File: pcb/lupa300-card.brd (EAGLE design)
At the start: 45.7 x 76.5 mm, 22 parts

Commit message: more work on lupa card
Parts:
- added C13, C14, C15, C16, C17, C18, C19, C20, C21, C22, C25, C26, C27, C28, C29, C30, C5, C6: (no value), rcl:C0603
- added C23, C24: (no value), rcl:C1206
- moved C7 18.8 mm to (19.1, 51.4), turned to 90 degrees
- moved R7 17.9 mm to (20.3, 51.4), turned to 90 degrees
- moved U$2 8.35 mm to (40.0, 71.8)
- moved U$4 8.28 mm to (36.2, 64.1)
- moved C2 7.24 mm to (32.4, 72.4)
- moved C1 7.24 mm to (32.4, 69.8)
- moved U$1 2.54 mm to (15.2, 30.5)
- moved U$3 1.27 mm to (37.5, 55.9)
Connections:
- new net N$2: C25.2, C27.2
- net 2.5V: now also U$1.P$10, U$1.P$2, U$1.P$4, U$1.P$8
- net GND: now also C13.2, C14.2, C15.2, C16.2, C17.2, C18.2, C19.2, C20.2, C21.2, C22.2, C23.2, C24.2, C26.2, C28.2, C29.2, C30.2, C5.2, C6.2
- net VADC: now also C20.1, C21.1, C22.1; no longer U$1.P$4
- net VDDA: now also C14.1, C15.1, C16.1; no longer U$1.P$8
- net VDDD: now also C13.1, C5.1, C6.1; no longer U$1.P$10
- net VDDO: now also C17.1, C18.1, C19.1; no longer U$1.P$2
- net VPIX: now also C25.1, C26.1, C27.1
- net VRAW: now also C23.1, C24.1
- net VRESET_1: now also C28.1, C29.1, C30.1

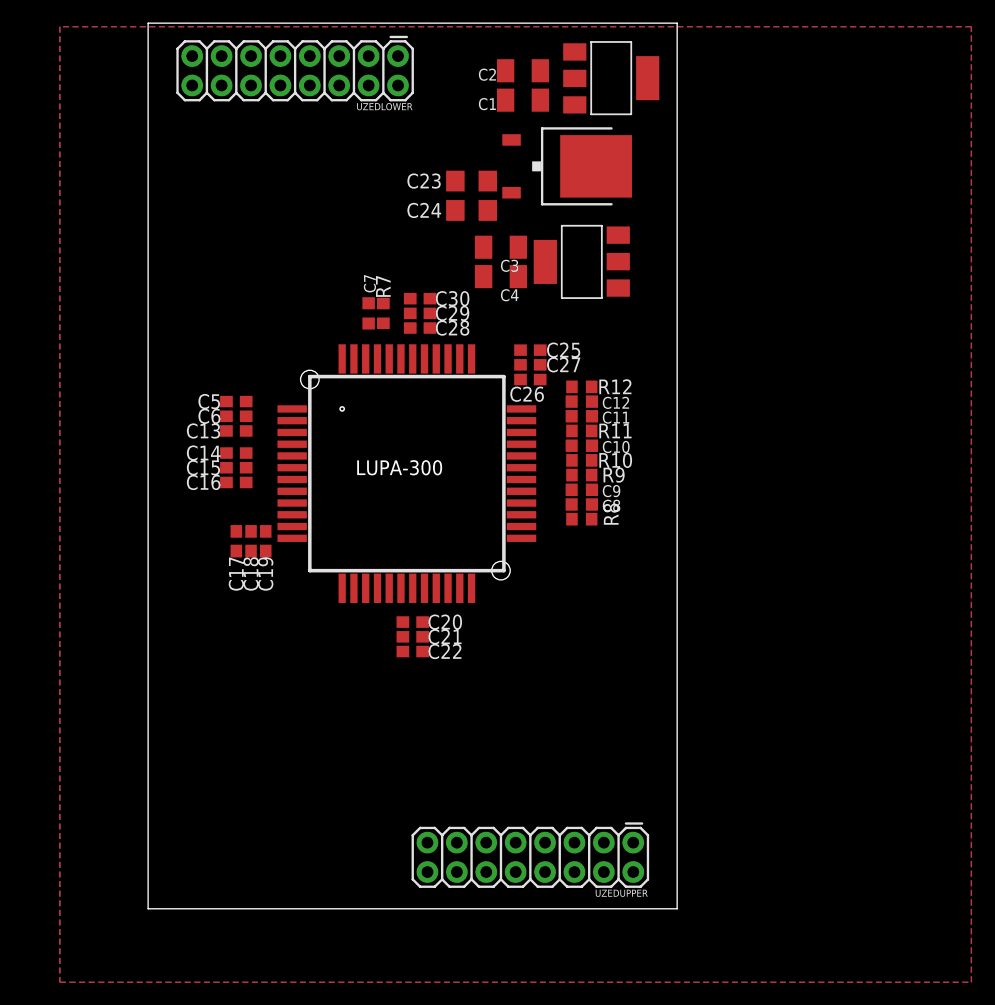
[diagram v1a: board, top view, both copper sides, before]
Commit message: made lupa card 4 layer
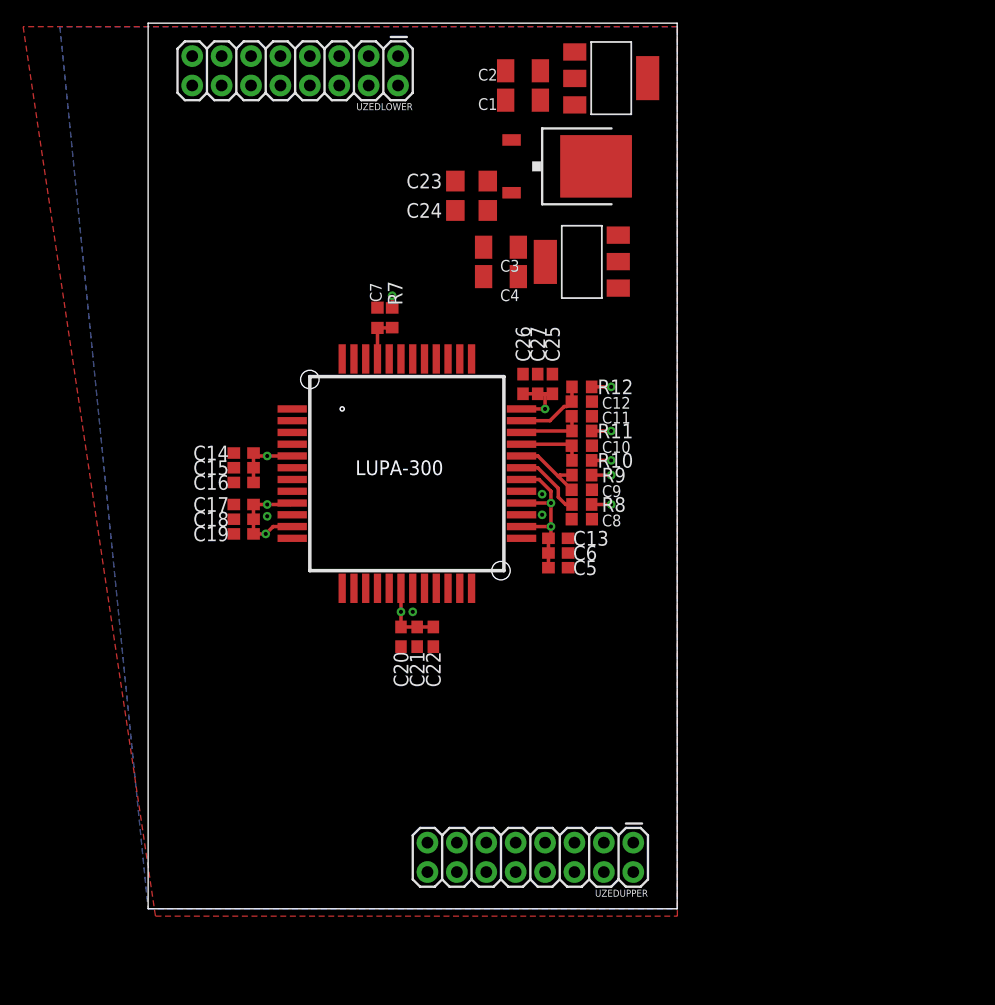
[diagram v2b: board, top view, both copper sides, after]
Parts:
- removed C28, C29, C30: (no value), rcl:C0603
- moved C5 31.3 mm to (35.4, 29.5), turned to 0 degrees
- moved C6 30.2 mm to (35.4, 30.7), turned to 0 degrees
- moved C13 29.3 mm to (35.4, 32.0), turned to 0 degrees
- moved C25 3.49 mm to (34.9, 45.3), turned to 90 degrees
- moved C17 3.24 mm to (8.26, 34.9), turned to 180 degrees
- moved C22 2.18 mm to (24.6, 23.5), turned to 270 degrees
- moved C18 2.01 mm to (8.26, 33.7), turned to 180 degrees
- moved C19 2.01 mm to (8.26, 32.4), turned to 180 degrees
- moved C27 1.77 mm to (33.7, 45.3), turned to 90 degrees
- moved C20 1.63 mm to (21.8, 23.5), turned to 270 degrees
- moved C8 1.27 mm to (37.5, 33.7)
- moved R8 1.27 mm to (37.5, 34.9)
- moved C7 0.85 mm to (19.8, 51.1)
- moved R7 0.85 mm to (21.1, 51.1), turned to 270 degrees
- moved C26 0.74 mm to (32.4, 45.3), turned to 90 degrees
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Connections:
- removed net N$2: C25.2, C27.2
- removed net VADC: C20.1, C21.1, C22.1, R8.1, U$1.P$21, U$1.P$30
- removed net VDDA: C14.1, C15.1, C16.1, R10.1, R11.1, R12.1, R9.1, U$1.P$19
- removed net VDDD: C13.1, C5.1, C6.1, U$1.P$23
- removed net VDDO: C17.1, C18.1, C19.1
- removed net VMEM_H: U$1.P$45
- removed net VPIX: C25.1, C26.1, C27.1, R7.1, U$1.P$13
- removed net VRESET_1: C28.1, C29.1, C30.1, U$1.P$43
- net 2.5V: now also C13.1, C14.1, C15.1, C16.1, C17.1, C18.1, C19.1, C20.1, C21.1, C22.1, C25.1, C26.1, C27.1, C5.1, C6.1, R10.1, R11.1, R12.1, R7.1, R8.1, R9.1, U$1.P$13, U$1.P$19, U$1.P$21, U$1.P$23, U$1.P$30
- net 3V3: now also U$1.P$43, U$1.P$45
- net GND: now also C25.2, C27.2; no longer C28.2, C29.2, C30.2
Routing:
- net 2.5V: track 0.00 -> 51.8 mm, vias 0 -> 13
- net BIAS4: track 0.00 -> 6.77 mm
- net BIAS1: track 0.00 -> 6.30 mm
- net ADC_BIAS: track 0.00 -> 6.12 mm
- net BIAS2: track 0.00 -> 5.69 mm
- net BIAS3: track 0.00 -> 5.66 mm
- net PRECHARGE_BIAS: track 0.00 -> 3.96 mm
- added copper zone on layer 2, net 2.5V
- added copper zone on layer 15, net 3V3

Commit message: finished prelim routing.
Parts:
- moved UZEDLOWER 67.9 mm to (21.5, 5.71)
- moved U$2 56.2 mm to (19.7, 19.3)
- moved U$4 55.2 mm to (17.7, 12.2)
- moved C23 55.1 mm to (8.13, 11.4), turned to 90 degrees
- moved C24 52.0 mm to (10.3, 11.4), turned to 90 degrees
- moved C2 50.2 mm to (19.2, 24.0)
- moved U$3 45.7 mm to (9.65, 19.6)
- moved C1 45.5 mm to (19.2, 26.3)
- moved C3 36.9 mm to (10.3, 26.3), turned to 0 degrees
- moved C4 36.7 mm to (10.3, 24.0), turned to 0 degrees
- moved C15 28.5 mm to (23.5, 62.2)
- moved C16 27.3 mm to (23.5, 59.4)
- moved C14 26.3 mm to (23.5, 60.8)
- moved C12 21.2 mm to (27.1, 62.2), turned to 45 degrees
- moved C11 19.8 mm to (29.0, 60.5), turned to 45 degrees
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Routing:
- net LINE_VALID: track 0.00 -> 69.0 mm
- net FRAME_VALID: track 0.00 -> 60.2 mm
- net INT_TIME3: track 0.00 -> 46.8 mm
- net CLK: track 0.00 -> 45.3 mm
- net RESET: track 0.00 -> 45.1 mm
- net D8: track 0.00 -> 44.9 mm
- net D6: track 0.00 -> 43.2 mm
- net D9: track 0.00 -> 41.7 mm
- net D4: track 0.00 -> 41.2 mm
- net INT_TIME1: track 0.00 -> 41.1 mm
- net INT_TIME2: track 0.00 -> 40.8 mm
- net D7: track 0.00 -> 40.7 mm
- net D2: track 0.00 -> 40.1 mm
- net D5: track 0.00 -> 39.8 mm
- net D0: track 0.00 -> 39.2 mm
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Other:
- board size 45.7 x 76.5 mm -> 45.7 x 65.7 mm

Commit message: routed critical signals.
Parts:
- added C28, C29: (no value), rcl:C0603
- moved C11 15.1 mm to (17.9, 50.2), flipped to the bottom, turned to 270 degrees
- moved R11 14.1 mm to (19.2, 50.2), flipped to the bottom, turned to 90 degrees
- moved C9 14.0 mm to (19.9, 57.3), turned to 90 degrees
- moved R10 13.4 mm to (20.4, 50.2), flipped to the bottom, turned to 90 degrees
- moved R7 13.1 mm to (16.9, 42.9), flipped to the bottom, turned to 0 degrees
- moved C7 13.0 mm to (16.9, 41.7), flipped to the bottom, turned to 180 degrees
- moved C8 12.6 mm to (23.7, 57.3), turned to 90 degrees
- moved C15 12.6 mm to (14.5, 53.5), flipped to the bottom, turned to 0 degrees
- moved R8 12.5 mm to (22.5, 57.3), turned to 270 degrees
- moved C14 12.5 mm to (14.5, 52.2), flipped to the bottom, turned to 0 degrees
- moved C17 12.4 mm to (21.8, 38.2), flipped to the bottom, turned to 90 degrees
- moved C21 12.4 mm to (27.7, 38.4), flipped to the bottom, turned to 90 degrees
- moved C10 12.2 mm to (21.7, 50.2), flipped to the bottom, turned to 270 degrees
- moved R12 12.2 mm to (16.5, 57.1), turned to 270 degrees
- moved C22 11.6 mm to (26.4, 38.4), flipped to the bottom, turned to 90 degrees
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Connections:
- net 3V3: now also C28.1, C29.1
- net GND: now also C28.2, C29.2
- net SPI_CLK: now also UZEDLOWER.14; no longer UZEDLOWER.3
- net SPI_DATA: now also UZEDLOWER.16; no longer UZEDLOWER.5
- net SPI_EN: now also UZEDLOWER.12; no longer UZEDLOWER.1
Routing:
- net LINE_VALID: track 69.0 -> 0.00 mm
- net FRAME_VALID: track 60.2 -> 0.00 mm
- net INT_TIME3: track 46.8 -> 0.00 mm
- net INT_TIME1: track 41.1 -> 0.00 mm
- net INT_TIME2: track 40.8 -> 0.00 mm
- net CLK: track 45.3 -> 30.2 mm
- net 2.5V: track 60.9 -> 74.4 mm, vias 17 -> 26
- net RESET: track 45.1 -> 32.7 mm
- net D9: track 41.7 -> 48.4 mm
- net D7: track 40.7 -> 46.4 mm
- net D8: track 44.9 -> 50.4 mm
- net D6: track 43.2 -> 48.6 mm
- net 3V3: track 17.0 -> 22.3 mm, vias 3 -> 7
- net D5: track 39.8 -> 44.6 mm
- net BIAS1: track 7.93 -> 4.30 mm
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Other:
- board size 45.7 x 65.7 mm -> 44.4 x 60.8 mm

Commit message: finalized design
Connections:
- net FRAME_VALID: now also UZEDLOWER.12; no longer UZEDLOWER.10
- net INT_TIME1: now also UZEDLOWER.9; no longer UZEDLOWER.11
- net INT_TIME2: now also UZEDLOWER.10; no longer UZEDLOWER.13
- net INT_TIME3: now also UZEDLOWER.11; no longer UZEDLOWER.15
- net LINE_VALID: now also UZEDLOWER.13; no longer UZEDLOWER.9
- net SPI_CLK: now also UZEDLOWER.15; no longer UZEDLOWER.14
- net SPI_DATA: now also UZEDLOWER.14; no longer UZEDLOWER.16
- net SPI_EN: now also UZEDLOWER.16; no longer UZEDLOWER.12
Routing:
- net SPI_EN: track 0.00 -> 52.6 mm
- net SPI_DATA: track 0.00 -> 51.0 mm
- net SPI_CLK: track 0.00 -> 48.7 mm
- net FRAME_VALID: track 0.00 -> 43.3 mm
- net INT_TIME2: track 0.00 -> 42.6 mm
- net LINE_VALID: track 0.00 -> 41.0 mm
- net INT_TIME1: track 0.00 -> 40.7 mm
- net INT_TIME3: track 0.00 -> 39.5 mm
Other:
- board text added: "Matt Ruffner LUPA300 v2"
